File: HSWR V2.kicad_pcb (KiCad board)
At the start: 4 copper layers, 152 x 139 mm, 137 parts, among them IC1 INA181, IC2 INA181, IC3 INA181, IC4 ADUM3054, IC5 ADuM4160, J1 IO, J10 SWD, J4 USB_B, J5 B+, J6 B-, J7 U, J8 V, J9 W, Q11 IXFK300N20X3, Q12 IXFK300N20X3, Q3 IXFK300N20X3, Q4 IXFK300N20X3, Q7 IXFK300N20X3, Q8 IXFK300N20X3, U1 STM32F405RGTx, U2 IRS2186, U3 IRS2186, U4 IRS2186, U5 AP1117-50, Y1 8MHz

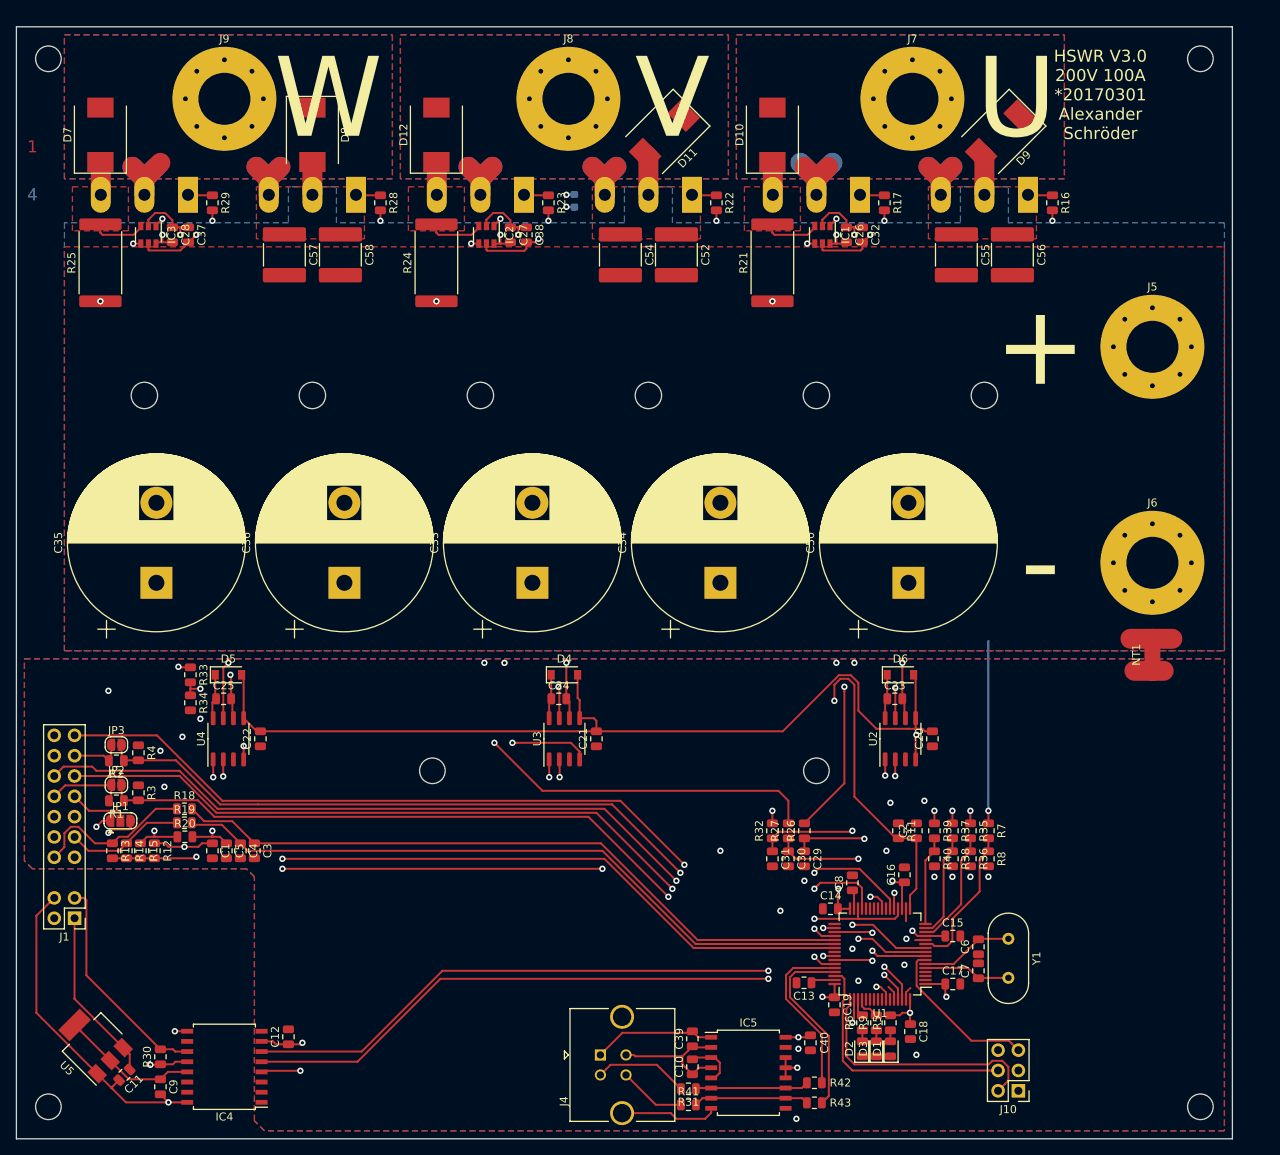
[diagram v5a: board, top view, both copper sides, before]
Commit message: - removed R2D.sch - selected PSUs - finished layout
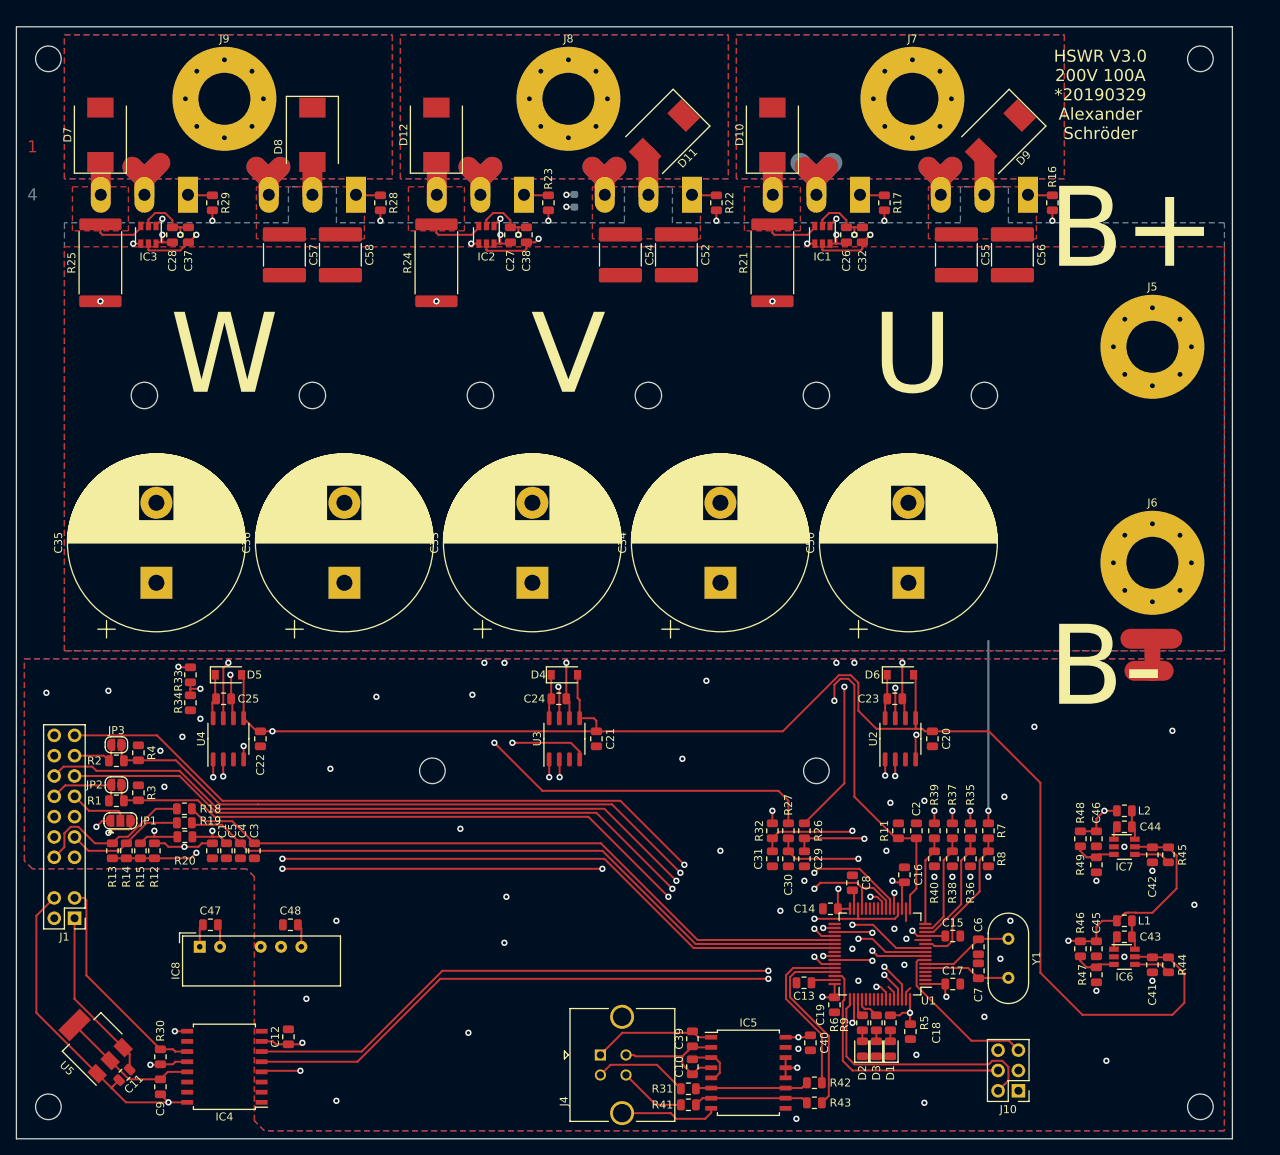
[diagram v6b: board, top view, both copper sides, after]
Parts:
- added C41: 22u, Capacitor_SMD:C_0805_2012Metric, F.Cu at (209.0, 141.2)
- added C42: 22u, Capacitor_SMD:C_0805_2012Metric, F.Cu at (209.0, 127.5)
- added C43: 100n, Capacitor_SMD:C_0805_2012Metric, F.Cu at (205.5, 137.8)
- added C44: 100n, Capacitor_SMD:C_0805_2012Metric, F.Cu at (205.5, 124.0)
- added C45: 22u, Capacitor_SMD:C_0805_2012Metric, F.Cu at (202.0, 139.2)
- added C46: 22u, Capacitor_SMD:C_0805_2012Metric, F.Cu at (202.0, 125.5)
- added C47: 2u2, Capacitor_SMD:C_0805_2012Metric, F.Cu at (91.2, 136.2)
- added C48: 2u2, Capacitor_SMD:C_0805_2012Metric, F.Cu at (101.2, 136.2)
- added IC6: JW5052C, Package_TO_SOT_SMD:TSOT-23-6, F.Cu at (205.5, 140.2)
- added IC7: JW5052C, Package_TO_SOT_SMD:TSOT-23-6, F.Cu at (205.5, 126.5)
- added IC8: B1212S-2W, Converter_DCDC:Converter_DCDC_muRata_NMAxxxxSC_THT, F.Cu at (89.9, 139.0)
- added L1: FCI201209F-4R7K, Inductor_SMD:L_0805_2012Metric, F.Cu at (205.5, 135.8)
- added L2: FCI201209F-4R7K, Inductor_SMD:L_0805_2012Metric, F.Cu at (205.5, 122.0)
- added R44: 100k, Resistor_SMD:R_0805_2012Metric, F.Cu at (211.0, 141.2)
- added R45: 100k, Resistor_SMD:R_0805_2012Metric, F.Cu at (211.0, 127.5)
- added R46: 110k, Resistor_SMD:R_0805_2012Metric, F.Cu at (200.0, 139.2)
- added R47: 15k, Resistor_SMD:R_0805_2012Metric, F.Cu at (202.0, 142.5)
- added R48: 49k9, Resistor_SMD:R_0805_2012Metric, F.Cu at (200.0, 125.5)
- added R49: 11k, Resistor_SMD:R_0805_2012Metric, F.Cu at (202.0, 128.8)
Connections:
- net /CAN bus transceiver/12V_ext renamed +12VA
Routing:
- net +5V: track 23.6 -> 177.0 mm, vias 1 -> 2
- net +12V: track 116.2 -> 219.0 mm, vias 0 -> 1
- net Earth: track 52.3 -> 78.4 mm
- net +12VA: track 21.8 -> 41.9 mm
- net +3V3: track 240.0 -> 246.8 mm, vias 18 -> 19
- net Net-(IC6-Pad3): track 0.00 -> 5.25 mm
- net Net-(IC7-Pad3): track 0.00 -> 5.25 mm
- net /MCU/TX_SCL_MOSI: track 110.9 -> 115.6 mm
- net Net-(IC6-Pad4): track 0.00 -> 4.60 mm
- net Net-(IC7-Pad4): track 0.00 -> 4.60 mm
- net Net-(C43-Pad2): track 0.00 -> 3.70 mm
- net Net-(C44-Pad2): track 0.00 -> 3.70 mm
- net Net-(C43-Pad1): track 0.00 -> 1.70 mm
- net Net-(C44-Pad1): track 0.00 -> 1.70 mm
- net /Filters/TEMP_IN: track 116.4 -> 117.5 mm
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- added copper zone on GND, net /Power MOSFETS/U
- added copper zone on GND, net /Power MOSFETS/V
- added copper zone on GND, net /Power MOSFETS/W
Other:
- board text added: "B+"
- board text added: "B-"
- board text added: "HSWR V3.0 200V 100A *20190329 Alexander Schröder"
- board text removed: "+"
- board text removed: "-"
- board text removed: "HSWR V3.0 200V 100A *20170301 Alexander Schröder"
